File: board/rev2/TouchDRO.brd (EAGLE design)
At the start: 50.8 x 50.8 mm, 27 parts

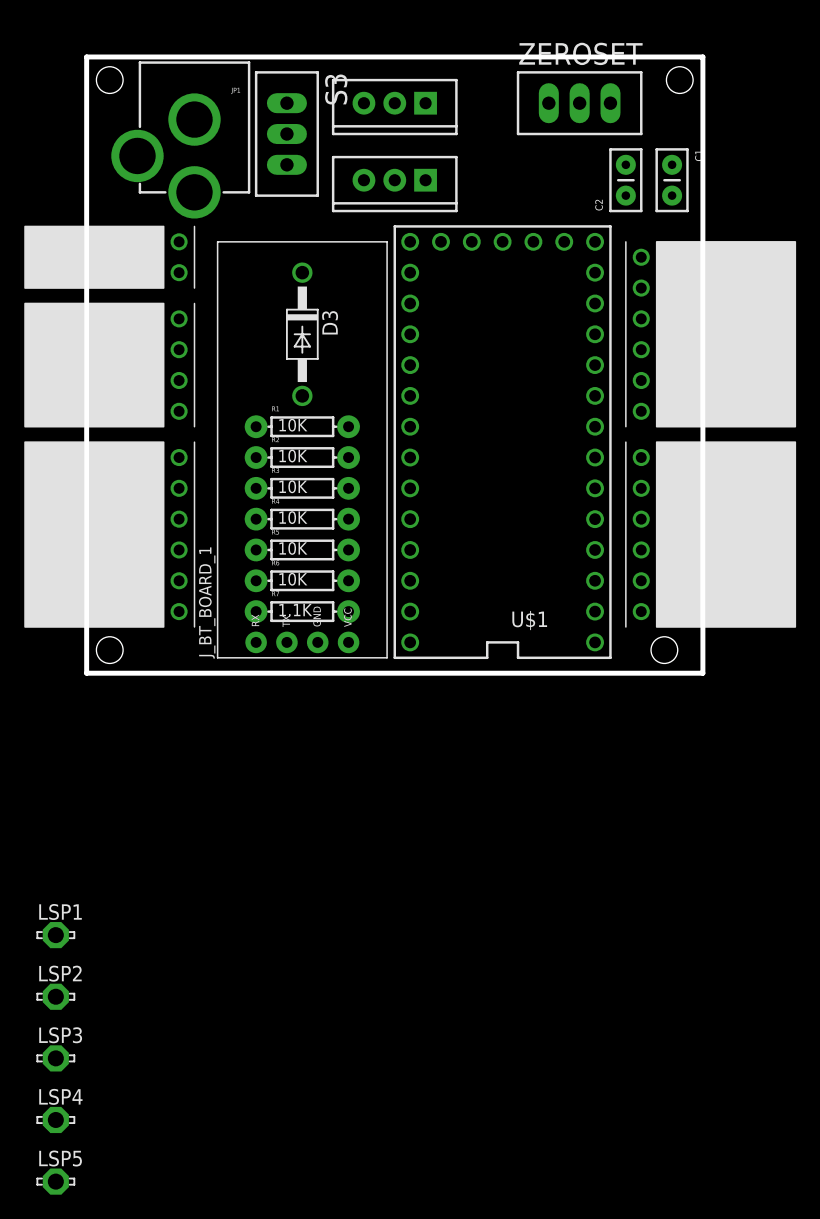
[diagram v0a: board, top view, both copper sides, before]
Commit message: adding rev2 dependencies and updates to the rev2 board
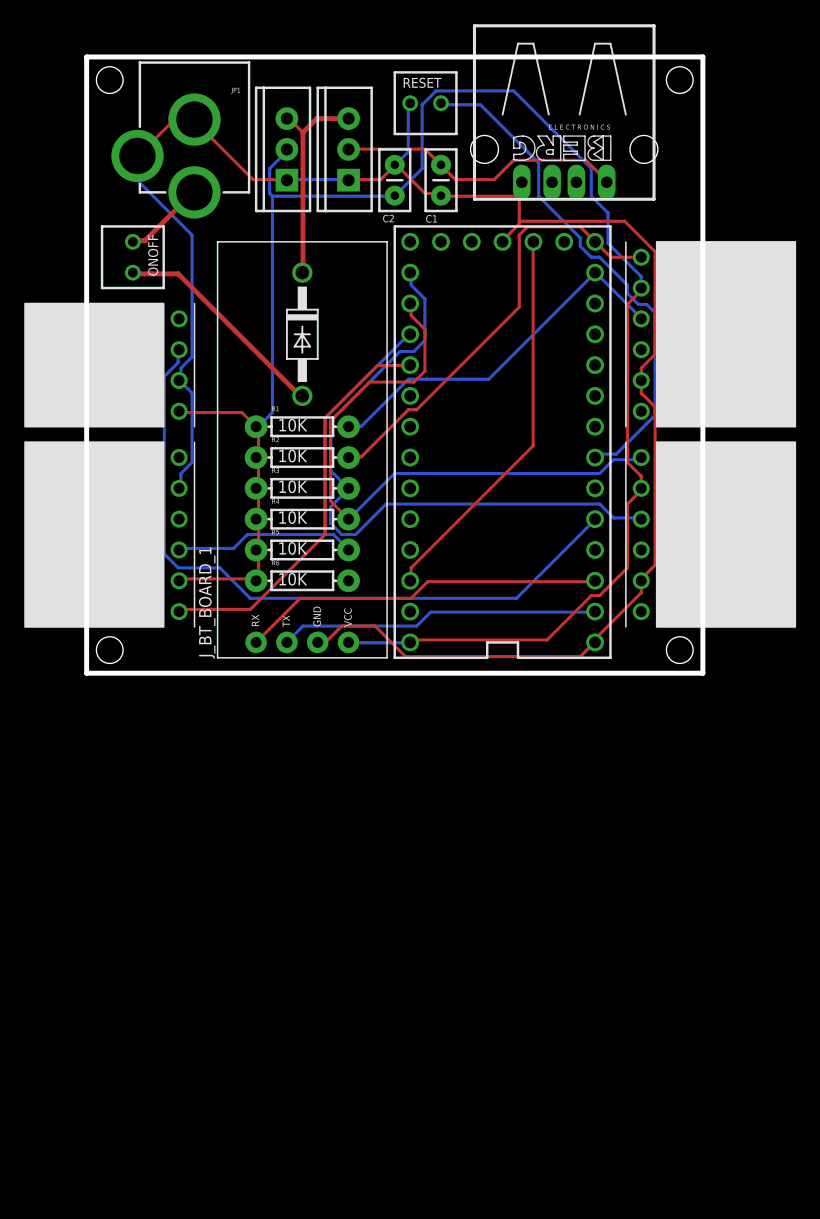
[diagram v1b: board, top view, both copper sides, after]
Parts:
- removed LDO33, LDO5: (no value), SparkFun-PowerIC:TO220-IGO
- removed LSP1, LSP2, LSP3, LSP4, LSP5: LSP13, solpad:LSP13
- removed R7: 1.1K, SparkFun-Passives:AXIAL-0.3EZ
- removed S3: TL36PO, switch:TL3XPO
- removed USBPOWER: KF2510_2PIN, KF2510:KF2510_2PIN
- removed ZEROSET: TL32PO, switch:TL3XPO
- added ONOFF: DS-228, Switches:DS-EXT
- added RESET: DS-227, Switches:DS-EXT
- added U2: VREG_33, regulators:TO220
- added U3: VREG_5, regulators:TO220
- added X1: (no value), con-berg:PN87520
- U$1: value TEENSY_3.1_BASIC -> TEENSY_3.2
- moved C2 19.1 mm to (25.4, 39.4)
- moved C1 19.0 mm to (29.2, 41.9)
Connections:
- removed net N$2: R7.P$2, ZEROSET.1
- net +3V3: now also U2.OUT; no longer LDO33.OUT, R7.P$1
- net +5V: now also U3.OUT, X1.1; no longer LDO5.OUT, USBPOWER.P$1
- net D1: now also U2.IN, U3.IN; no longer LDO33.IN, LDO5.IN
- net GND: now also RESET.P$1, U2.GND, U3.GND, X1.4; no longer LDO33.GND, LDO5.GND, USBPOWER.P$2, ZEROSET.3
- net N$6: now also ONOFF.P$1; no longer S3.2
- net ONOFF: now also ONOFF.P$2; no longer S3.3
- net ZSET: now also RESET.P$2; no longer ZEROSET.2
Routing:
- net GND: track 0.00 -> 152.0 mm
- net +3V3: track 0.00 -> 148.7 mm
- net T: track 0.00 -> 57.1 mm
- net Y_A: track 0.00 -> 53.9 mm
- net Y_B: track 0.00 -> 50.6 mm
- net ZSET: track 0.00 -> 42.1 mm
- net X_B: track 0.00 -> 36.5 mm
- net Z_A: track 0.00 -> 34.5 mm
- net Z_B: track 0.00 -> 33.1 mm
- net 3.3V: track 0.00 -> 32.1 mm
- net X_A: track 0.00 -> 31.0 mm
- net TR: track 0.00 -> 30.0 mm
- net RCV: track 0.00 -> 26.5 mm
- net +5V: track 0.00 -> 23.8 mm
- net ONOFF: track 0.00 -> 18.2 mm
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
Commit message: tweaks to board and layout. added dxf output of board layout
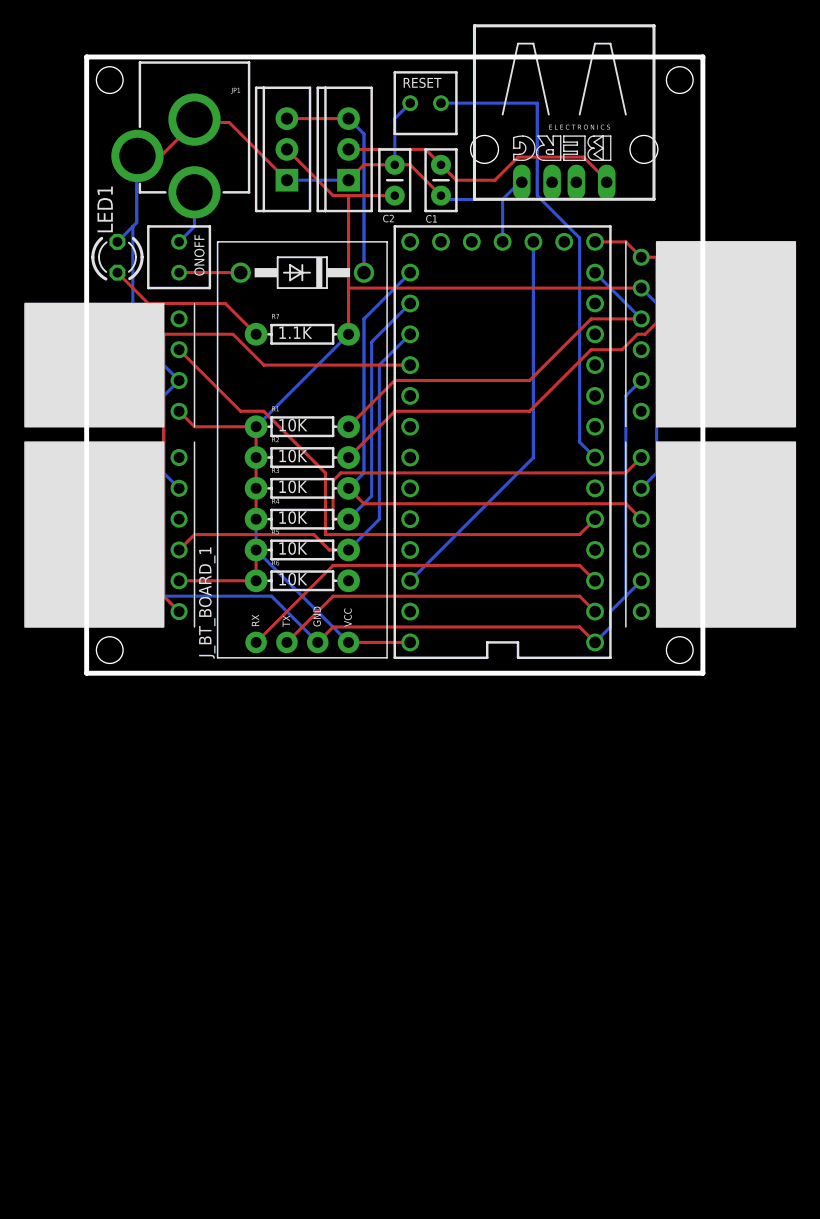
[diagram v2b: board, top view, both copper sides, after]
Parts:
- added LED1: (no value), led:LED3MM
- added R7: 1.1K, SparkFun-Passives:AXIAL-0.3EZ
- moved D3 5.08 mm to (17.8, 33.0), turned to 180 degrees
- moved ONOFF 3.81 mm to (7.62, 33.0)
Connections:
- new net N$1: LED1.A, R7.P$1
- net +3V3: now also R7.P$2
- net GND: now also LED1.K
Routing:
- net +3V3: track 148.7 -> 116.1 mm
- net N$1: track 0.00 -> 13.5 mm
- net ONOFF: track 18.2 -> 5.08 mm
- net T: track 57.1 -> 44.1 mm
- net Z_B: track 33.1 -> 44.8 mm
- net Y_A: track 53.9 -> 45.1 mm
- net X_B: track 36.5 -> 41.0 mm
- net ZSET: track 42.1 -> 39.1 mm
- net X_A: track 31.0 -> 33.2 mm
- net N$6: track 6.76 -> 4.61 mm
- net TR: track 30.0 -> 31.1 mm
- net RCV: track 26.5 -> 27.5 mm
- net D1: track 17.6 -> 18.3 mm

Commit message: added usb type-a connector. add power supply cap.
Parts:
- removed X1: (no value), con-berg:PN87520
- added C3: 100uF, SparkFun-Passives:CAP-PTH-SMALLEZ
- added USB_PWR_OUT: (no value), USB:USBTYPEA
- moved U2 1.91 mm to (16.5, 41.3)
- moved U3 1.91 mm to (21.6, 41.3)
- renumbered RESET to ZEROSET
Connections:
- removed net Z_C: R6.P$2
- net +5V: now also USB_PWR_OUT.1; no longer X1.1
- net GND: now also C3.2, USB_PWR_OUT.4; no longer X1.4
- net ONOFF: now also C3.1
- net Z_B: now also R6.P$2
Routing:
- net Z_B: track 44.8 -> 64.6 mm
- net ONOFF: track 5.08 -> 22.7 mm
- net GND: track 151.9 -> 168.1 mm
- net D1: track 18.3 -> 16.4 mm
- net +5V: track 24.1 -> 24.9 mm
- net +3V3: track 116.1 -> 115.4 mm
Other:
- board text added: "For use with Sherline 8220/8225 Only"
